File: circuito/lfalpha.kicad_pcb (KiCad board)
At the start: 2 copper layers, 200 x 100 mm, 52 parts, among them J1 BAT, J2 ANALOG, J3 MotorA, J4 MotorB, J5 Bluetooth, J6 REMOTE S/S, J7 SPI, J8 SENSOR CON, J9 SENSOR BAR, SW1 ON/OFF, SW2 START, SW3 STOP, U1 AruinoNano, U2 DRV8835-Carrier, U3 QRE1113, U4 QRE1113, U5 QRE1113, U6 QRE1113, U7 QRE1113, U8 QRE1113

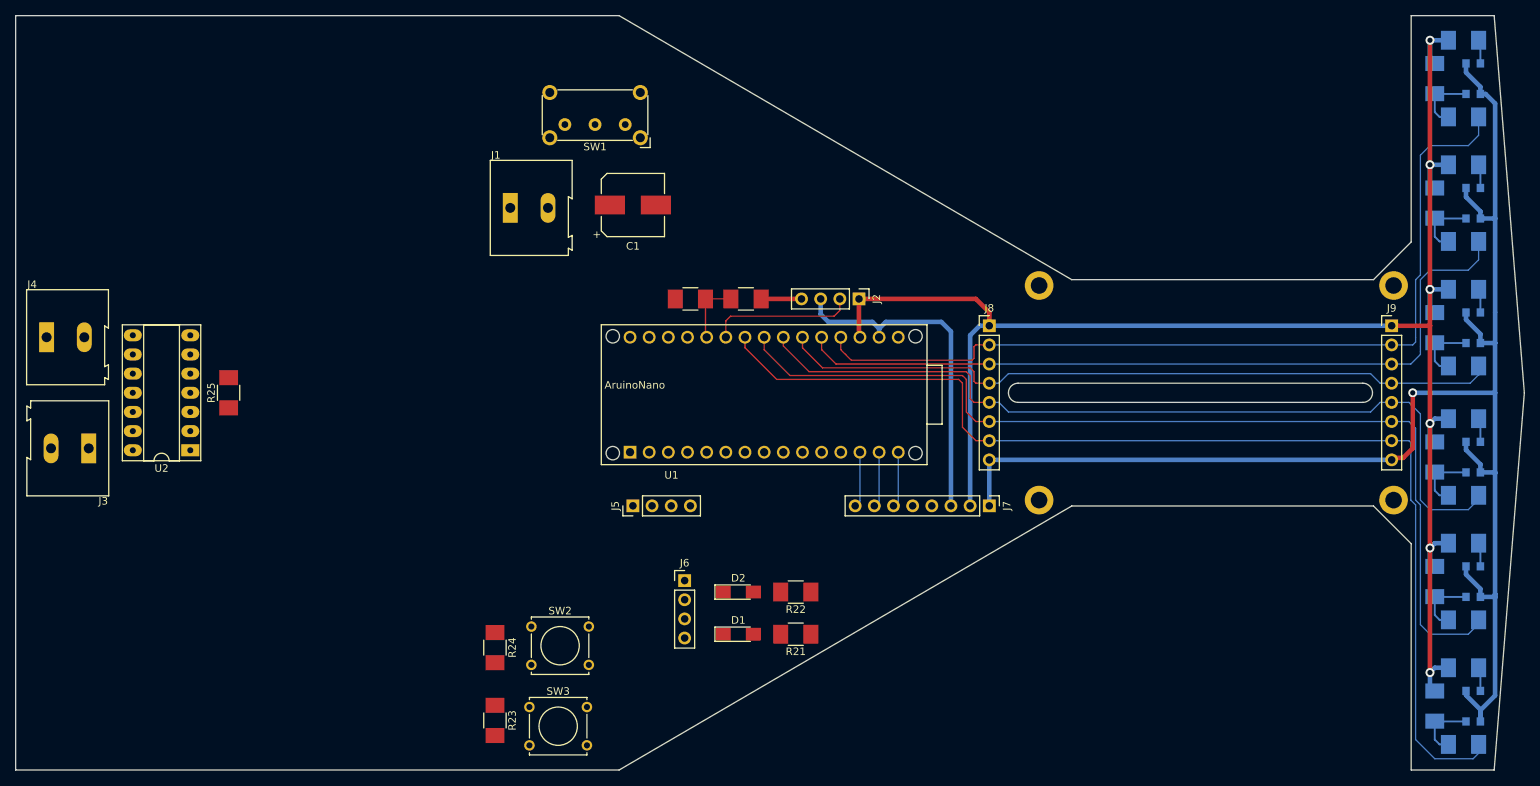
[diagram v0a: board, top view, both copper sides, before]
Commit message: Modificato il footprint dell'interruttore ed aggiunti i fori di fissaggio per i motori
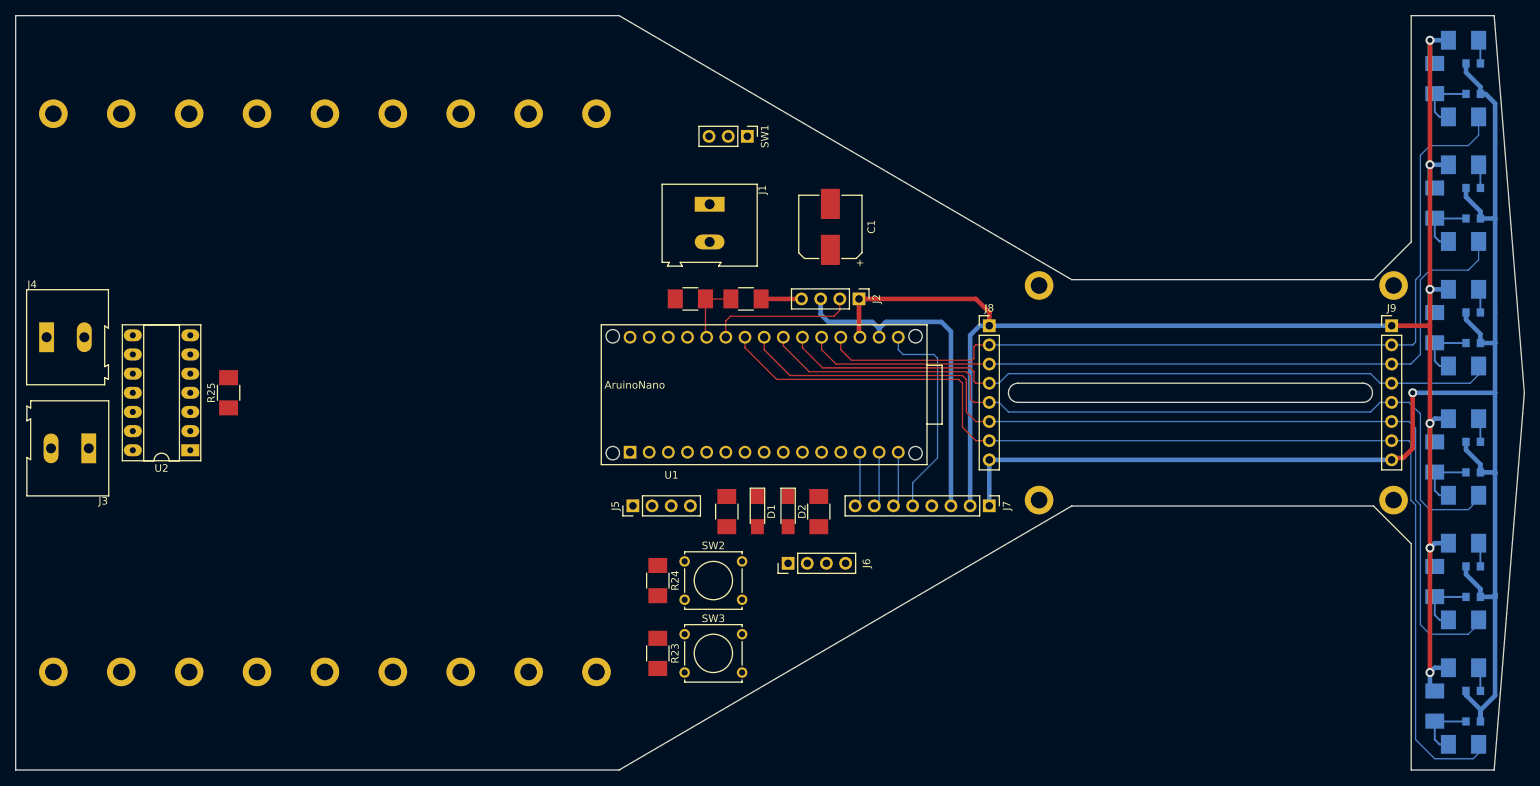
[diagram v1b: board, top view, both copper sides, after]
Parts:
- added REF**: MountingHole_2.2mm_M2_DIN965_Pad, Mounting_Holes:MountingHole_2.2mm_M2_DIN965_Pad, F.Cu at (127.0, 132.0)
- added REF**: MountingHole_2.2mm_M2_DIN965_Pad, Mounting_Holes:MountingHole_2.2mm_M2_DIN965_Pad, F.Cu at (55.0, 58.0)
- added REF**: MountingHole_2.2mm_M2_DIN965_Pad, Mounting_Holes:MountingHole_2.2mm_M2_DIN965_Pad, F.Cu at (64.0, 58.0)
- added REF**: MountingHole_2.2mm_M2_DIN965_Pad, Mounting_Holes:MountingHole_2.2mm_M2_DIN965_Pad, F.Cu at (100.0, 58.0)
- added REF**: MountingHole_2.2mm_M2_DIN965_Pad, Mounting_Holes:MountingHole_2.2mm_M2_DIN965_Pad, F.Cu at (127.0, 58.0)
- added REF**: MountingHole_2.2mm_M2_DIN965_Pad, Mounting_Holes:MountingHole_2.2mm_M2_DIN965_Pad, F.Cu at (55.0, 132.0)
- added REF**: MountingHole_2.2mm_M2_DIN965_Pad, Mounting_Holes:MountingHole_2.2mm_M2_DIN965_Pad, F.Cu at (64.0, 132.0)
- added REF**: MountingHole_2.2mm_M2_DIN965_Pad, Mounting_Holes:MountingHole_2.2mm_M2_DIN965_Pad, F.Cu at (109.0, 132.0)
- added REF**: MountingHole_2.2mm_M2_DIN965_Pad, Mounting_Holes:MountingHole_2.2mm_M2_DIN965_Pad, F.Cu at (82.0, 132.0)
- added REF**: MountingHole_2.2mm_M2_DIN965_Pad, Mounting_Holes:MountingHole_2.2mm_M2_DIN965_Pad, F.Cu at (100.0, 132.0)
- added REF**: MountingHole_2.2mm_M2_DIN965_Pad, Mounting_Holes:MountingHole_2.2mm_M2_DIN965_Pad, F.Cu at (118.0, 132.0)
- added REF**: MountingHole_2.2mm_M2_DIN965_Pad, Mounting_Holes:MountingHole_2.2mm_M2_DIN965_Pad, F.Cu at (91.0, 132.0)
- added REF**: MountingHole_2.2mm_M2_DIN965_Pad, Mounting_Holes:MountingHole_2.2mm_M2_DIN965_Pad, F.Cu at (73.0, 132.0)
- added REF**: MountingHole_2.2mm_M2_DIN965_Pad, Mounting_Holes:MountingHole_2.2mm_M2_DIN965_Pad, F.Cu at (118.0, 58.0)
- added REF**: MountingHole_2.2mm_M2_DIN965_Pad, Mounting_Holes:MountingHole_2.2mm_M2_DIN965_Pad, F.Cu at (109.0, 58.0)
- added REF**: MountingHole_2.2mm_M2_DIN965_Pad, Mounting_Holes:MountingHole_2.2mm_M2_DIN965_Pad, F.Cu at (91.0, 58.0)
- added REF**: MountingHole_2.2mm_M2_DIN965_Pad, Mounting_Holes:MountingHole_2.2mm_M2_DIN965_Pad, F.Cu at (82.0, 58.0)
- added REF**: MountingHole_2.2mm_M2_DIN965_Pad, Mounting_Holes:MountingHole_2.2mm_M2_DIN965_Pad, F.Cu at (73.0, 58.0)
- SW1: footprint Buttons_Switches_ThroughHole:SW_E-Switch_EG1224_SPDT_Angled -> Socket_Strips:Socket_Strip_Straight_1x03_Pitch2.54mm
- moved J1 26.4 mm to (142.0, 70.0), turned to 270 degrees
- moved C1 26.3 mm to (158.0, 73.0), turned to 90 degrees
- moved R23 23.3 mm to (135.1, 129.5)
- moved R24 23.3 mm to (135.1, 119.9)
- moved SW3 22.7 mm to (138.7, 127.0)
- moved SW2 22.1 mm to (138.7, 117.3)
- moved R21 18.7 mm to (144.3, 110.7), turned to 270 degrees
- moved D1 16.5 mm to (148.3, 110.7), turned to 270 degrees
- moved SW1 16.3 mm to (147.0, 61.0), turned to 270 degrees
- moved J6 13.9 mm to (152.4, 117.6), turned to 90 degrees
- moved D2 12.5 mm to (152.4, 110.7), turned to 270 degrees
- moved R22 11.1 mm to (156.5, 110.7), turned to 270 degrees
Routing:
- net Net-(J7-Pad5): track 0.00 -> 28.3 mm

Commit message: Completato il disegno del PCB, a meno di verifiche
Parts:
- D1: value STATUS1 -> S1
- D2: value STATUS2 -> S2
- R25: moved to B.Cu
- moved R25 9.23 mm to (69.0, 95.0)
- moved SW1 9.06 mm to (138.0, 62.0), turned to 90 degrees
- moved J5 0.83 mm to (131.0, 110.0)
- moved D1 0.71 mm to (149.0, 111.0), turned to 90 degrees
- moved D2 0.47 mm to (152.0, 111.0), turned to 90 degrees
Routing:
- net GND: track 209.7 -> 443.2 mm, vias 1 -> 4
- net +5V: track 226.4 -> 409.2 mm, vias 6 -> 8
- net +BATT: track 0.00 -> 138.1 mm
- net Net-(U1-Pad11): track 0.00 -> 92.0 mm
- net Net-(U1-Pad10): track 0.00 -> 87.1 mm
- net Net-(U1-Pad9): track 0.00 -> 84.7 mm, vias 0 -> 1
- net Net-(U1-Pad8): track 0.00 -> 79.8 mm
- net Net-(J6-Pad4): track 0.00 -> 63.0 mm
- net Net-(J6-Pad3): track 0.00 -> 45.3 mm
- net Net-(J1-Pad2): track 0.00 -> 19.6 mm
- net Net-(J3-Pad2): track 0.00 -> 16.9 mm
- net Net-(J4-Pad1): track 0.00 -> 14.9 mm
- net Net-(J3-Pad1): track 0.00 -> 9.63 mm
- net Net-(R25-Pad2): track 0.00 -> 8.82 mm
- net Net-(J4-Pad2): track 0.00 -> 8.14 mm
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
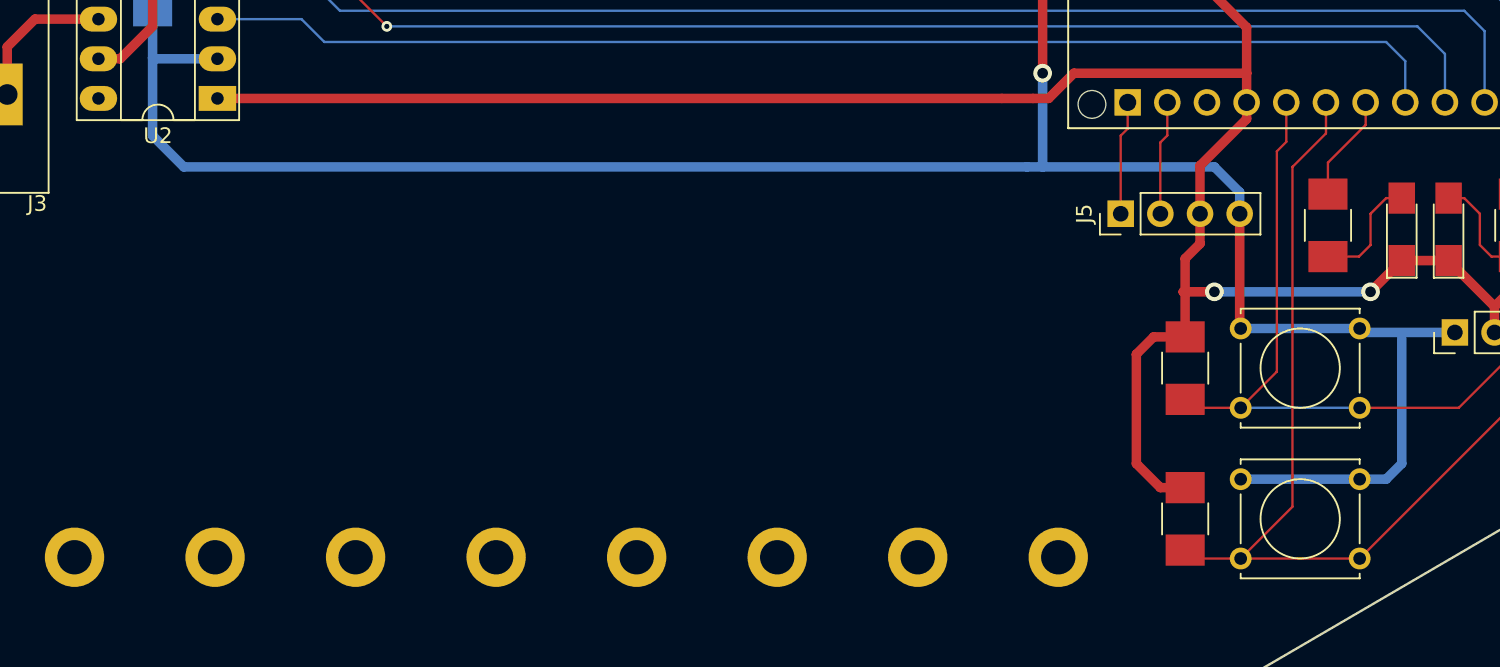
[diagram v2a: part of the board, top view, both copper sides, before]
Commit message: Mancavano due collegamenti, riscontrati con il DRC, spostate due resistenze per garantire uno dei collegamenti mancanti. Generati i file Gerber, da verificare se le impostazioni usate vanno bene.
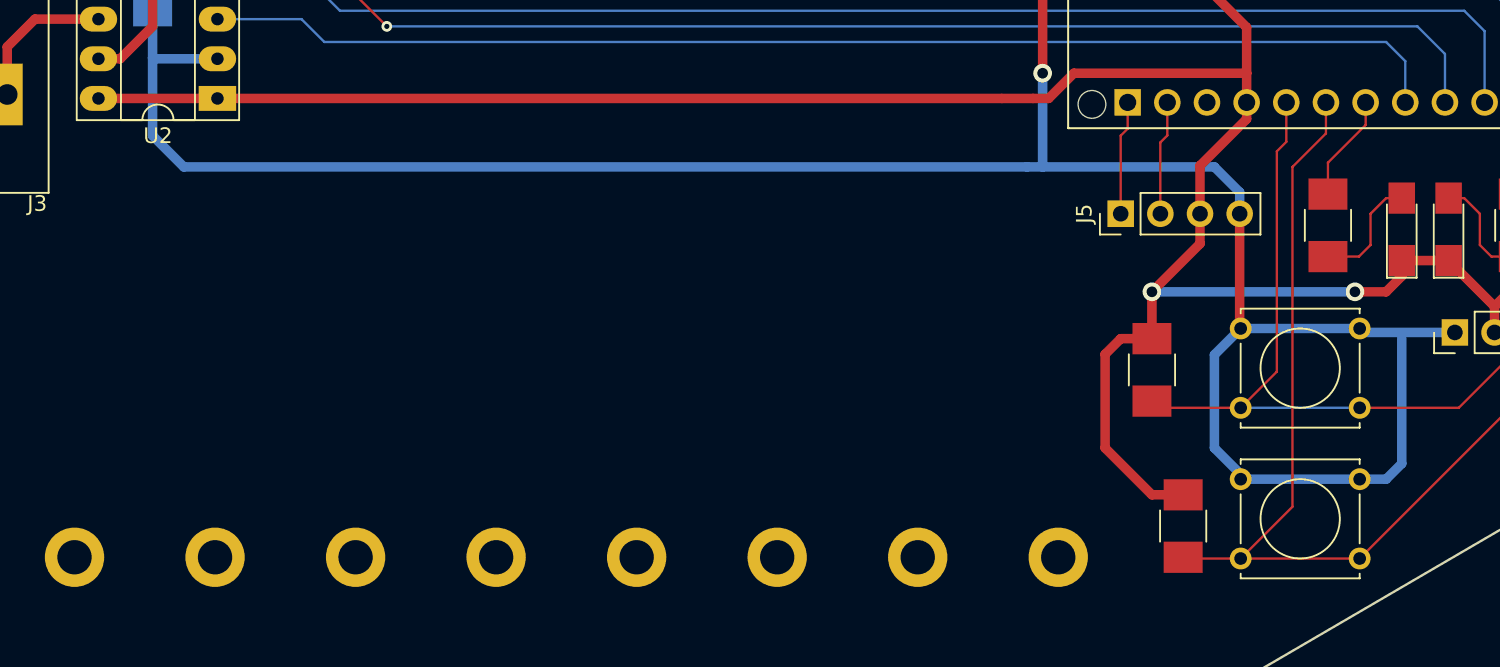
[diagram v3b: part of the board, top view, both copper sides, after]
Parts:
- moved R24 2.13 mm to (133.0, 120.0)
- moved R23 0.48 mm to (135.0, 130.0)
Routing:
- net GND: track 443.2 -> 456.6 mm
- net +5V: track 409.2 -> 420.3 mm
- net Net-(J6-Pad3): track 45.3 -> 47.4 mm
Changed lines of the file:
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@@
   (general
     (links 126)
-    (no_connects 2)
+    (no_connects 0)
     (area 40.480914 44.7802 250.100001 145.0848)
     (thickness 1.6)
     (drawings 22)
-    (tracks 457)
+    (tracks 461)
     (zones 0)
     (modules 70)
@@
     (visible_elements 7FFFFF7F)
     (pcbplotparams
-      (layerselection 0x00030_80000001)
+      (layerselection 0x011fc_80000001)
       (usegerberextensions false)
       (excludeedgelayer true)
@@
       (outputformat 1)
       (mirror false)
-      (drillshape 1)
+      (drillshape 0)
       (scaleselection 1)
       (outputdirectory ""))
@@
   )
   (module Resistors_SMD:R_1210_HandSoldering (layer F.Cu)
-    (at 135.128 129.54 270)
+    (at 135 130 270)
     (descr "Resistor SMD 1210, hand soldering")
     (tags "resistor 1210")
@@
   )
   (module Resistors_SMD:R_1210_HandSoldering (layer F.Cu)
-    (at 135.128 119.888 270)
+    (at 133 120 270)
     (descr "Resistor SMD 1210, hand soldering")
     (tags "resistor 1210")
@@
       (effects (font (size 1 1) (thickness 0.15)))
     )
-    (fp_text value ANALOG (at 0 9.95 270) (layer F.Fab)
+    (fp_text value ANALOG (at -2.55 0.798 360) (layer F.Fab)
       (effects (font (size 1 1) (thickness 0.15)))
     )
@@
       (effects (font (size 1 1) (thickness 0.15)))
     )
-    (fp_text value ON/OFF (at 0 7.41 90) (layer F.Fab)
+    (fp_text value ON/OFF (at 3 2 180) (layer F.Fab)
       (effects (font (size 1 1) (thickness 0.15)))
     )
@@
   (segment (start 140.54 64.46) (end 137 68) (width 0.6096) (layer F.Cu) (net 1))
   (segment (start 137 82.104) (end 137.446 82.55) (width 0.6096) (layer F.Cu) (net 1))
+  (segment (start 135 128) (end 133 128) (width 0.6096) (layer F.Cu) (net 2))
+  (segment (start 131 118) (end 133 118) (width 0.6096) (layer F.Cu) (net 2))
+  (segment (start 130 119) (end 131 118) (width 0.6096) (layer F.Cu) (net 2))
+  (segment (start 130 125) (end 130 119) (width 0.6096) (layer F.Cu) (net 2))
+  (segment (start 133 128) (end 130 125) (width 0.6096) (layer F.Cu) (net 2))
+  (segment (start 132 118) (end 133 118) (width 0.6096) (layer F.Cu) (net 2))
+  (segment (start 149 113) (end 149 114) (width 0.6096) (layer F.Cu) (net 2))
+  (segment (start 149 114) (end 148 115) (width 0.6096) (layer F.Cu) (net 2))
+  (via (at 133 115) (size 1.1938) (drill 0.6858) (layers F.Cu B.Cu) (net 2))
+  (segment (start 146 115) (end 133 115) (width 0.6096) (layer B.Cu) (net 2))
+  (via (at 146 115) (size 1.1938) (drill 0.6858) (layers F.Cu B.Cu) (net 2))
+  (segment (start 148 115) (end 146 115) (width 0.6096) (layer F.Cu) (net 2))
+  (segment (start 136.08 110) (end 136.08 111.92) (width 0.6096) (layer F.Cu) (net 2))
+  (segment (start 133 115) (end 133 118) (width 0.6096) (layer F.Cu) (net 2))
+  (segment (start 136.08 111.92) (end 133 115) (width 0.6096) (layer F.Cu) (net 2))
+  (segment (start 73.152 102.616) (end 65.532 102.616) (width 0.6096) (layer F.Cu) (net 2))
   (segment (start 149 113) (end 152 113) (width 0.6096) (layer F.Cu) (net 2))
   (segment (start 125.384 102.616) (end 126.384 102.616) (width 0.6096) (layer F.Cu) (net 2))
@@
   (segment (start 133.985 92.985) (end 133.985 87.63) (width 0.6096) (layer F.Cu) (net 2))
   (segment (start 139.065 98.065) (end 133.985 92.985) (width 0.6096) (layer F.Cu) (net 2))
-  (segment (start 149 113) (end 147 115) (width 0.6096) (layer F.Cu) (net 2))
-  (segment (start 137 115) (end 135.128 115) (width 0.6096) (layer F.Cu) (net 2))
-  (via (at 137 115) (size 1.1938) (drill 0.6858) (layers F.Cu B.Cu) (net 2))
-  (segment (start 147 115) (end 137 115) (width 0.6096) (layer B.Cu) (net 2))
-  (via (at 147 115) (size 1.1938) (drill 0.6858) (layers F.Cu B.Cu) (net 2))
-  (segment (start 135.128 115) (end 135 115) (width 0.6096) (layer F.Cu) (net 2))
-  (segment (start 135 115) (end 135.128 115) (width 0.6096) (layer F.Cu) (net 2))
   (segment (start 179.07 109.982) (end 179.07 111.93) (width 0.6096) (layer F.Cu) (net 2))
   (segment (start 155.88 115) (end 154.94 115.94) (width 0.6096) (layer F.Cu) (net 2))
@@
   (segment (start 136.08 106.92) (end 136.08 110) (width 0.6096) (layer F.Cu) (net 2))
   (segment (start 139.065 103.935) (end 136.08 106.92) (width 0.6096) (layer F.Cu) (net 2))
-  (segment (start 136.08 110) (end 136.08 111.92) (width 0.6096) (layer F.Cu) (net 2))
-  (segment (start 135.128 112.872) (end 135.128 115) (width 0.6096) (layer F.Cu) (net 2))
-  (segment (start 135.128 115) (end 135.128 117.888) (width 0.6096) (layer F.Cu) (net 2))
-  (segment (start 136.08 111.92) (end 135.128 112.872) (width 0.6096) (layer F.Cu) (net 2))
-  (segment (start 135.128 127.54) (end 133.54 127.54) (width 0.6096) (layer F.Cu) (net 2))
-  (segment (start 133.112 117.888) (end 135.128 117.888) (width 0.6096) (layer F.Cu) (net 2))
-  (segment (start 132 119) (end 133.112 117.888) (width 0.6096) (layer F.Cu) (net 2))
-  (segment (start 132 126) (end 132 119) (width 0.6096) (layer F.Cu) (net 2))
-  (segment (start 133.54 127.54) (end 132 126) (width 0.6096) (layer F.Cu) (net 2))
   (segment (start 155 80) (end 152 80) (width 0.6096) (layer F.Cu) (net 2))
   (segment (start 134 82) (end 134 87.615) (width 0.6096) (layer B.Cu) (net 2))
@@
   (segment (start 147 73) (end 147 64) (width 0.6096) (layer B.Cu) (net 5))
   (segment (start 145 75) (end 147 73) (width 0.6096) (layer B.Cu) (net 5))
+  (segment (start 138.684 127) (end 138.684 126.684) (width 0.6096) (layer B.Cu) (net 6))
+  (segment (start 138.684 126.684) (end 137 125) (width 0.6096) (layer B.Cu) (net 6))
+  (segment (start 137 119.032) (end 138.684 117.348) (width 0.6096) (layer B.Cu) (net 6))
+  (segment (start 137 125) (end 137 119.032) (width 0.6096) (layer B.Cu) (net 6))
   (segment (start 138 90) (end 128 90) (width 0.6096) (layer B.Cu) (net 6))
   (segment (start 139.065 88.935) (end 138 90) (width 0.6096) (layer B.Cu) (net 6))
@@
   (segment (start 133.54 105.43) (end 133.54 110) (width 0.1524) (layer F.Cu) (net 13))
   (segment (start 133.985 104.985) (end 133.54 105.43) (width 0.1524) (layer F.Cu) (net 13))
+  (segment (start 138.684 122.428) (end 133.428 122.428) (width 0.1524) (layer F.Cu) (net 14))
+  (segment (start 133.428 122.428) (end 133 122) (width 0.1524) (layer F.Cu) (net 14))
   (segment (start 146.304 122.428) (end 152.654 122.428) (width 0.1524) (layer F.Cu) (net 14))
   (segment (start 152.654 122.428) (end 157.48 117.602) (width 0.1524) (layer F.Cu) (net 14))
@@
   (segment (start 141 106) (end 141 120.112) (width 0.1524) (layer F.Cu) (net 14))
   (segment (start 141.605 105.395) (end 141 106) (width 0.1524) (layer F.Cu) (net 14))
-  (segment (start 138.684 122.428) (end 135.668 122.428) (width 0.1524) (layer F.Cu) (net 14))
-  (segment (start 135.668 122.428) (end 135.128 121.888) (width 0.1524) (layer F.Cu) (net 14))
+  (segment (start 138.684 132.08) (end 135.08 132.08) (width 0.1524) (layer F.Cu) (net 15))
+  (segment (start 135.08 132.08) (end 135 132) (width 0.1524) (layer F.Cu) (net 15))
   (segment (start 160.02 117.602) (end 160.02 118.364) (width 0.1524) (layer F.Cu) (net 15))
   (segment (start 160.02 118.364) (end 146.304 132.08) (width 0.1524) (layer F.Cu) (net 15))
@@
   (segment (start 144.145 104.855) (end 142 107) (width 0.1524) (layer F.Cu) (net 15))
   (segment (start 138.684 132.08) (end 146.304 132.08) (width 0.1524) (layer F.Cu) (net 15))
-  (segment (start 138.684 132.08) (end 135.668 132.08) (width 0.1524) (layer F.Cu) (net 15))
-  (segment (start 135.668 132.08) (end 135.128 131.54) (width 0.1524) (layer F.Cu) (net 15))
   (segment (start 167.005 87.63) (end 167.005 89.281) (width 0.1524) (layer B.Cu) (net 17))
   (segment (start 168.91 106.934) (end 168.91 109.982) (width 0.1524) (layer B.Cu) (net 17))
